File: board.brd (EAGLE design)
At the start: 69.8 x 50.8 mm, 85 parts, among them J1 AVR_SPI_PRG_6NS, U1 VS1063DS, U2 USD-SOCKETNEW, U3 MAX1555, U4 TPS2112A, U6 74HC595, U7 3.3V, U8 1.8V, Y1 12.288MHz, Y2 8MHz

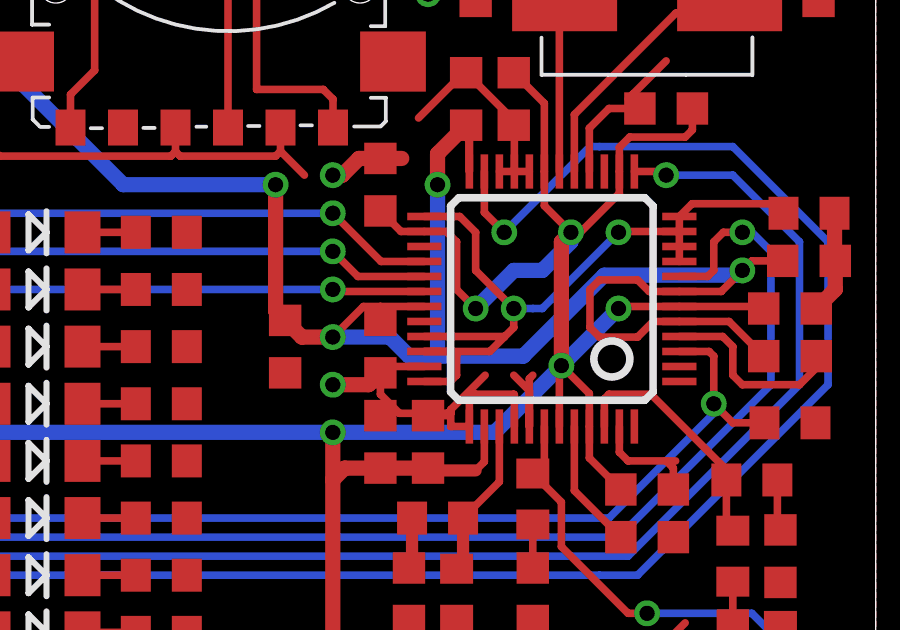
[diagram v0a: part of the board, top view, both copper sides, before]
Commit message: Connected XTest on vs1063 to VDD
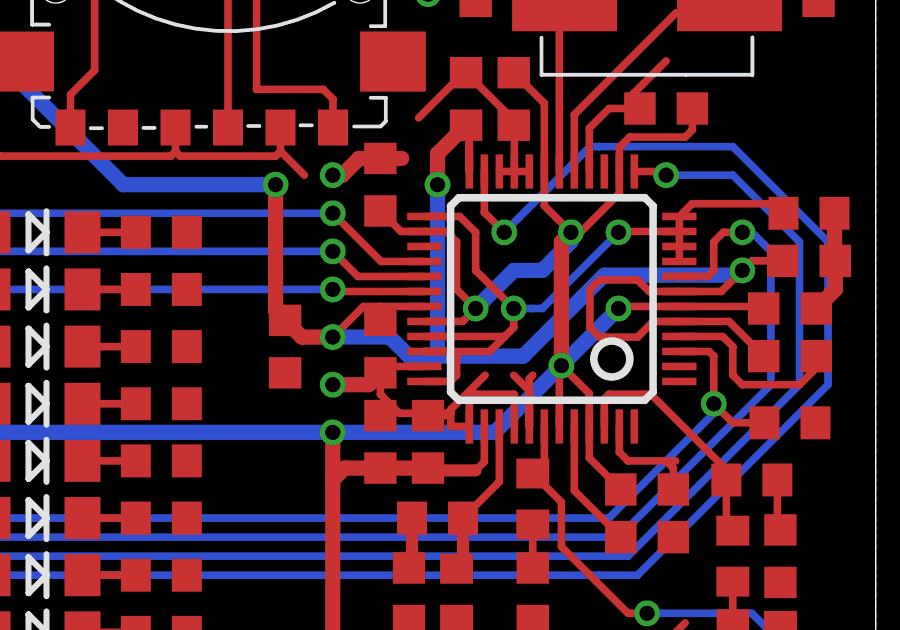
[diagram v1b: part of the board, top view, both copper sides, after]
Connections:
- removed net MP3_XTEST: U1.32
- net VDD: now also U1.32
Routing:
- net VDD: track 199.8 -> 201.7 mm
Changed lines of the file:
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@@
 <wire x1="30.695" y1="23.1775" x2="30.7975" y2="23.1775" width="0.254" layer="1"/>
 <wire x1="30.7975" y1="23.1775" x2="30.7975" y2="24.525" width="0.254" layer="1"/>
+<contactref element="U1" pad="32"/>
+<wire x1="54.805" y1="28.46" x2="56.0825" y2="28.46" width="0.254" layer="1"/>
+<wire x1="56.0825" y1="28.46" x2="56.515" y2="28.8925" width="0.254" layer="1"/>
 </signal>
 <signal name="GPIO">
@@
 <wire x1="28.995" y1="23.05" x2="28.995" y2="23.1775" width="0.254" layer="1"/>
 </signal>
-<signal name="MP3_XTEST">
-<contactref element="U1" pad="32"/>
-</signal>
 </signals>

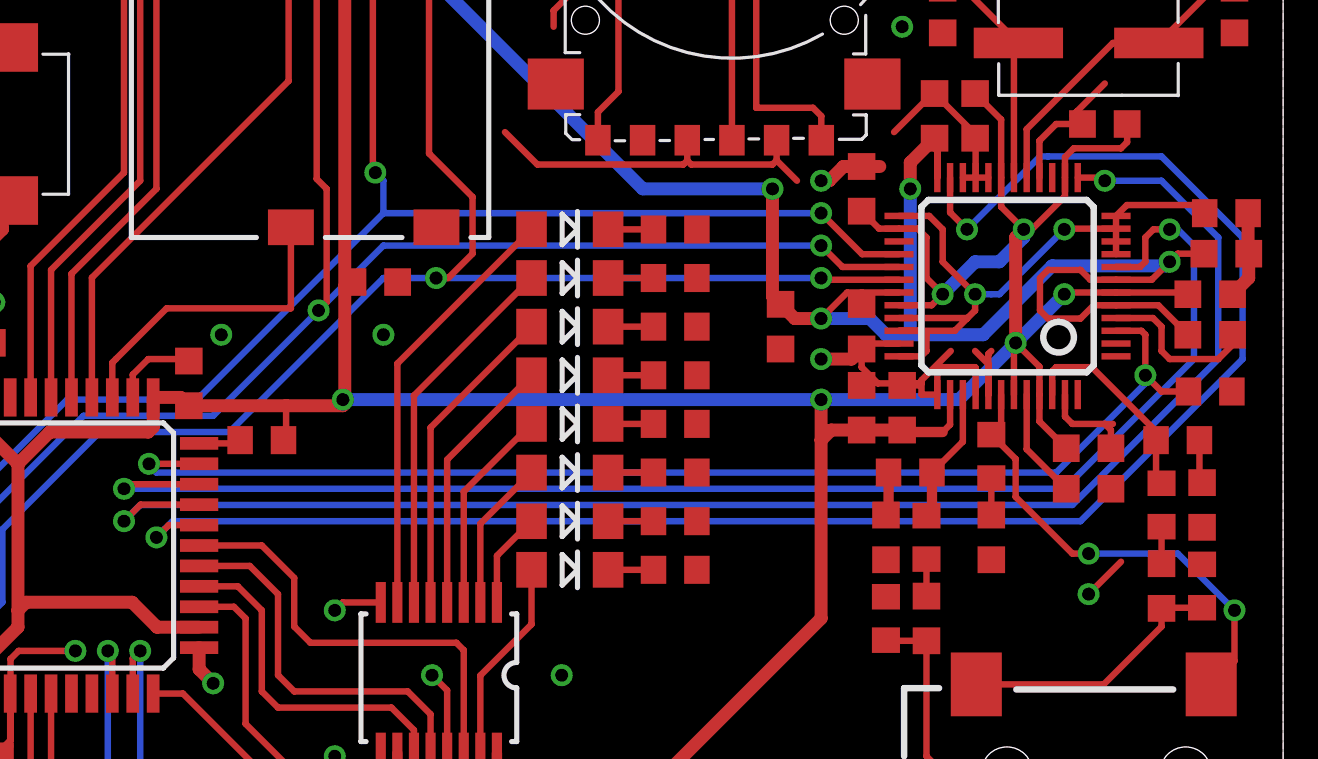
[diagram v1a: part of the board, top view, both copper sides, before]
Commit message: Added pull-ups to mp3 cs lines
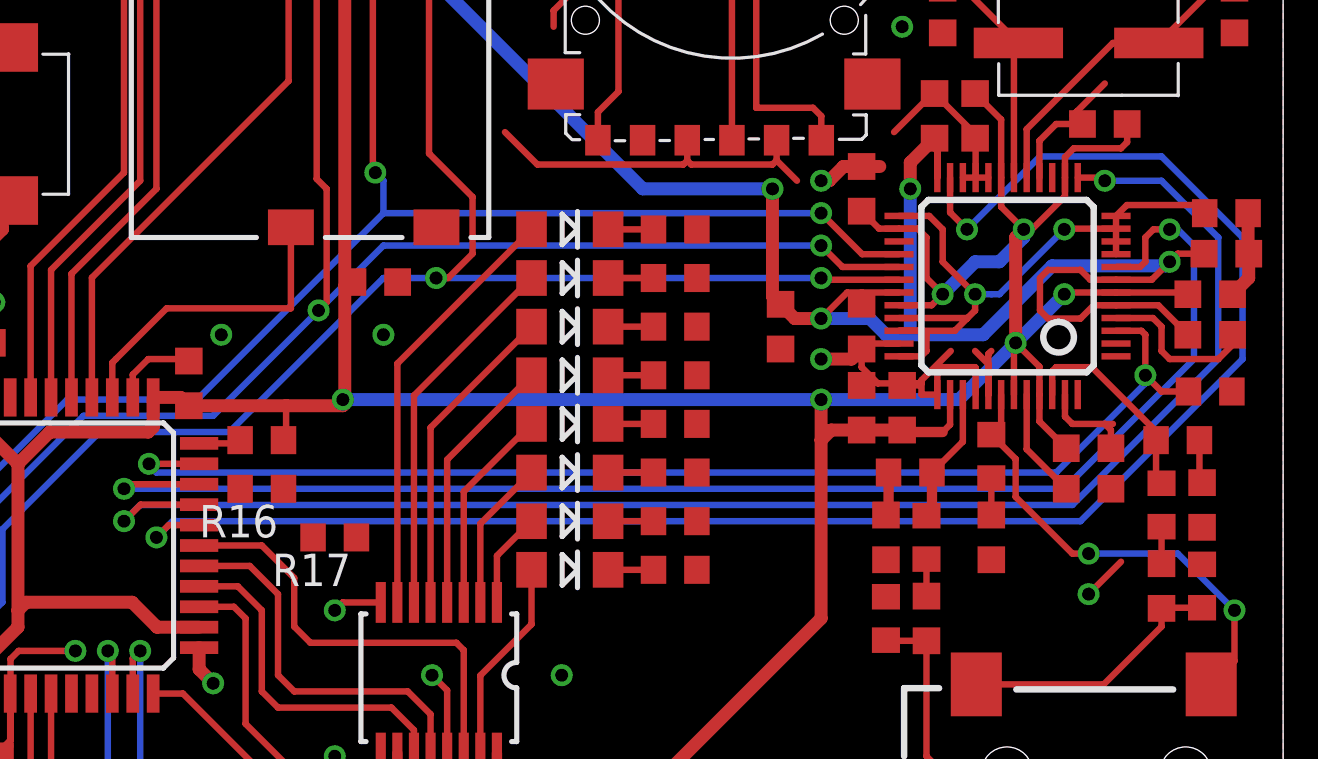
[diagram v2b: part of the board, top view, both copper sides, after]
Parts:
- added R16, R17: 10k, rcl:R0603W
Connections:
- net MP3_XCS: now also R16.1
- net MP3_XDCS: now also R17.1
- net VDD: now also R16.2, R17.2
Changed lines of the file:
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@@
 <element name="R14" library="rcl" package="R0603" value="10k" x="29.845" y="23.1775" smashed="yes" rot="R180"/>
 <element name="C33" library="rcl" package="C0603K" value="1u" x="50.165" y="27.6225" smashed="yes" rot="R270"/>
+<element name="R16" library="rcl" package="R0603W" value="10k" x="29.845" y="21.2725" rot="R180"/>
+<element name="R17" library="rcl" package="R0603W" value="10k" x="32.7025" y="19.3675" rot="R180"/>
 </elements>
 <signals>
@@
 <wire x1="54.805" y1="28.46" x2="56.0825" y2="28.46" width="0.254" layer="1"/>
 <wire x1="56.0825" y1="28.46" x2="56.515" y2="28.8925" width="0.254" layer="1"/>
+<contactref element="R17" pad="2"/>
+<contactref element="R16" pad="2"/>
+<wire x1="28.995" y1="21.2725" x2="31.8525" y2="19.3675" width="0" layer="19" extent="1-1"/>
+<wire x1="30.695" y1="23.1775" x2="28.995" y2="21.2725" width="0" layer="19" extent="1-1"/>
 </signal>
 <signal name="GPIO">
@@
 <wire x1="56.805" y1="32.095" x2="57.4675" y2="31.4325" width="0.254" layer="1"/>
 <via x="57.4675" y="31.4325" extent="1-16" drill="0.508"/>
-<wire x1="60.6425" y1="34.29" x2="65.0875" y2="34.29" width="0.254" layer="16"/>
+<wire x1="60.325" y1="34.29" x2="65.0875" y2="34.29" width="0.254" layer="16"/>
 <wire x1="65.0875" y1="34.29" x2="68.2625" y2="31.115" width="0.254" layer="16"/>
 <wire x1="68.2625" y1="31.115" x2="68.2625" y2="26.3525" width="0.254" layer="16"/>
@@
 <wire x1="26.2" y1="19.85" x2="25.7175" y2="19.3675" width="0.254" layer="1"/>
 <via x="25.7175" y="19.3675" extent="1-16" drill="0.508"/>
-<wire x1="25.7175" y1="19.3675" x2="26.035" y2="19.685" width="0.254" layer="16"/>
-<wire x1="26.035" y1="19.685" x2="26.3525" y2="20.0025" width="0.254" layer="16"/>
-<wire x1="26.3525" y1="20.0025" x2="60.6425" y2="20.0025" width="0.254" layer="16"/>
-<wire x1="60.6425" y1="20.0025" x2="61.9125" y2="20.0025" width="0.254" layer="16"/>
+<wire x1="25.7175" y1="19.3675" x2="26.3525" y2="20.0025" width="0.254" layer="16"/>
+<wire x1="26.3525" y1="20.0025" x2="61.9125" y2="20.0025" width="0.254" layer="16"/>
 <wire x1="61.9125" y1="20.0025" x2="68.2625" y2="26.3525" width="0.254" layer="16"/>
-<wire x1="60.6425" y1="34.29" x2="60.325" y2="34.29" width="0.254" layer="16"/>
 <wire x1="60.325" y1="34.29" x2="57.4675" y2="31.4325" width="0.254" layer="16"/>
+<contactref element="R16" pad="1"/>
+<wire x1="27.39" y1="19.85" x2="30.695" y2="21.2725" width="0" layer="19" extent="1-1"/>
 </signal>
 <signal name="MP3_XDCS">
@@
 <wire x1="27.39" y1="20.65" x2="25.095" y2="20.65" width="0.254" layer="1"/>
 <wire x1="25.095" y1="20.65" x2="24.4475" y2="20.0025" width="0.254" layer="1"/>
+<contactref element="R17" pad="1"/>
+<wire x1="27.39" y1="20.65" x2="33.5525" y2="19.3675" width="0" layer="19" extent="1-1"/>
 </signal>
 <signal name="MP3_DREQ">

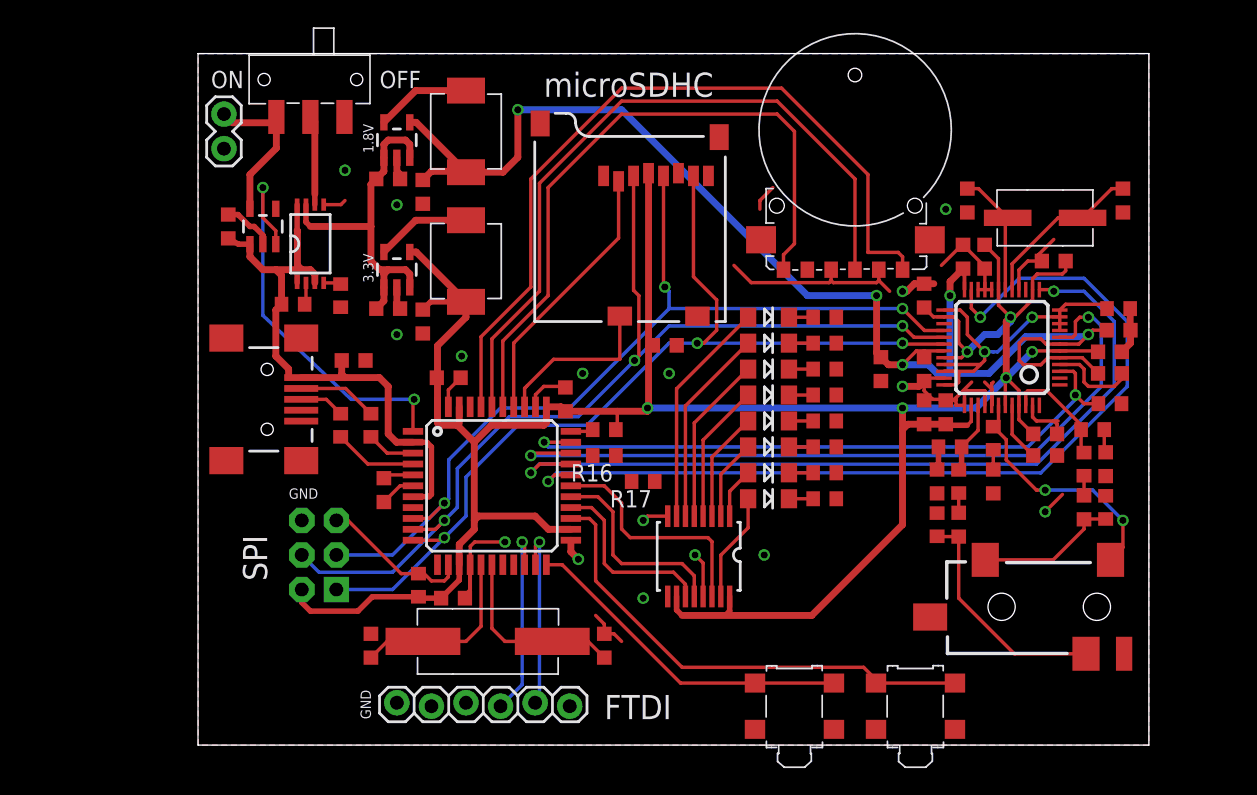
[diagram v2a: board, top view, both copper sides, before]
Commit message: Beginning to switch to atmega32u2
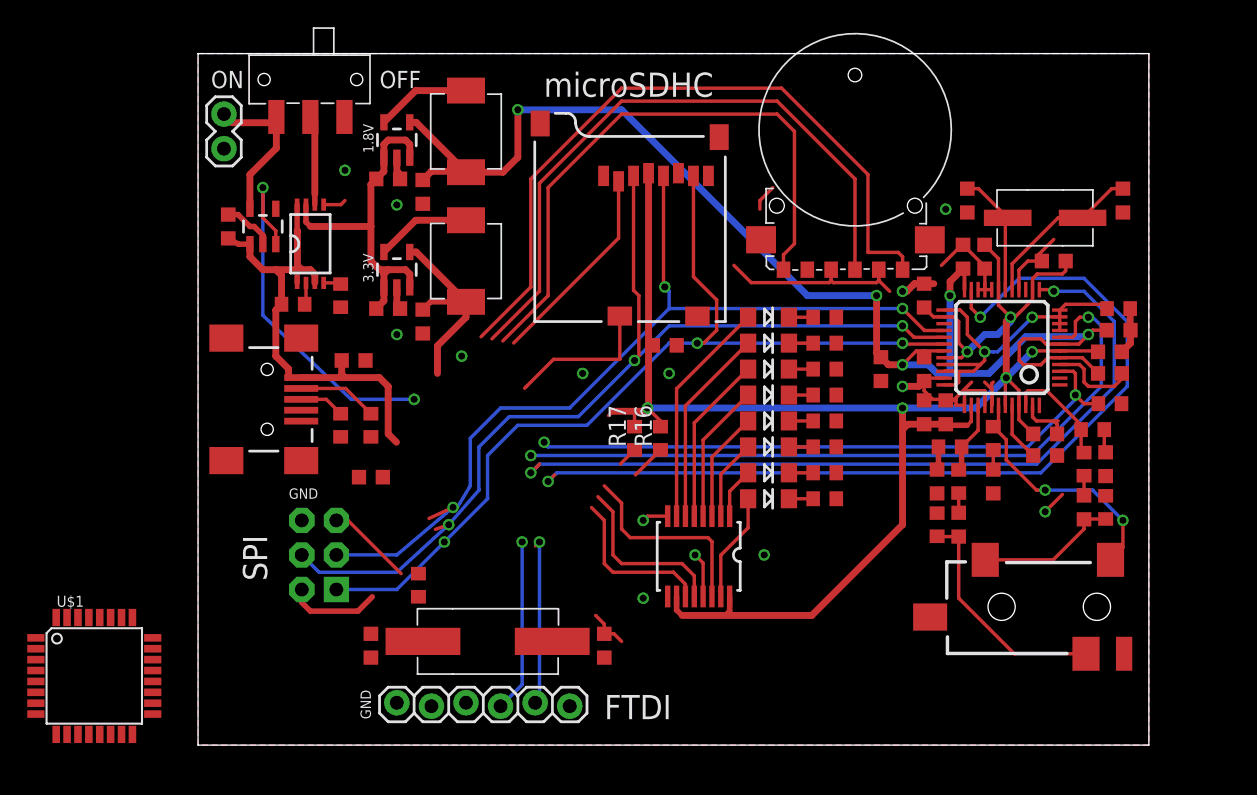
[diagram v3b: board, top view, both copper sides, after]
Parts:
- removed C23, C24, C32: 0.1u, rcl:C0603K
- removed R14: 10k, rcl:R0603
- removed S2, S3: EVQ-PSC, mkmp3:EVQ-PSQ
- removed U$2: ATMEGA32U4TQFP, SparkFun-DigitalIC:SPARKFUN-DIGITALIC_TQFP44
- added U$1: ATMEGA32U2, CEDT:TQFP32-08
- moved R16 4.32 mm to (34.0, 22.5), turned to 90 degrees
- moved R17 3.24 mm to (32.1, 22.5), turned to 90 degrees
- moved C17 1.35 mm to (12.7, 19.7), turned to 0 degrees
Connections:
- removed net N$15: JP2.3, U$2.20
- removed net N$16: JP2.2, U$2.21
- removed net N$38: R14.2, U$2.33
- removed net N$9: C17.1, U$2.6
- removed net SWITCH1: S2.A, S2.A', U$2.22
- removed net SWITCH2: S3.A, S3.A', U$2.25
- new net SERIAL_RX: JP2.3, U$1.8
- new net SERIAL_TX: JP2.2, U$1.9
- net CHG_B: no longer U$2.1
- net DS: no longer U$2.28
- net ENCODER_A: no longer U$2.38
- net ENCODER_B: no longer U$2.40
- net ENCODER_S: no longer U$2.39
- net GND: now also U$1.28, U$1.3; no longer C23.2, C24.2, C32.2, S2.B, S2.B', S3.B, S3.B', U$2.15, U$2.23, U$2.35, U$2.43, U$2.5
- net MISO: now also U$1.17; no longer U$2.11
- net MOSI: now also U$1.16; no longer U$2.10
- net MP3_DREQ: no longer U$2.31
- net MP3_XCS: no longer U$2.29
- net MP3_XDCS: no longer U$2.30
- net MP3_XRESET: no longer U$2.32
- net N$14: now also U$1.2, Y2.P$1; no longer U$2.16, Y2.P$2
- net N$2: now also U$1.1, Y2.P$2; no longer U$2.17, Y2.P$1
- net RESET: now also R11.1, U$1.24; no longer R11.2, U$2.13
- net SCK: now also U$1.15; no longer U$2.9
- net SD_CD: no longer U$2.36
- net SD_CS: now also U$1.14; no longer U$2.37
- net SHCP: no longer U$2.26
- net STCP: no longer U$2.27
- net USB_D+: no longer U$2.4
- net USB_D-: no longer U$2.3
- net VBUS: now also U$1.31; no longer U$2.2, U$2.7
- net VDD: now also C17.1, R11.2, U$1.27, U$1.32, U$1.4; no longer C23.1, C24.1, C32.1, R11.1, R14.1, U$2.14, U$2.24, U$2.34, U$2.42, U$2.44
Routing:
- net VDD: track 201.7 -> 157.8 mm
- net SWITCH2: track 35.8 -> 0.00 mm
- net SWITCH1: track 24.7 -> 0.00 mm
- net GND: track 102.9 -> 83.9 mm, vias 16 -> 14
- net N$15: track 14.5 -> 0.00 mm, vias 1 -> 0
- net N$2: track 13.8 -> 0.00 mm
- net N$16: track 13.7 -> 0.00 mm, vias 1 -> 0
- net N$14: track 13.6 -> 0.00 mm
- net SERIAL_RX: track 0.00 -> 13.0 mm, vias 0 -> 1
- net SERIAL_TX: track 0.00 -> 12.4 mm, vias 0 -> 1
- net VBUS: track 44.0 -> 36.4 mm
- net USB_D+: track 6.14 -> 0.00 mm
- net ENCODER_B: track 57.8 -> 52.6 mm
- net ENCODER_S: track 52.6 -> 47.6 mm
- net ENCODER_A: track 48.8 -> 44.0 mm
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
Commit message: Switched to smaller uC and VS1003 chip
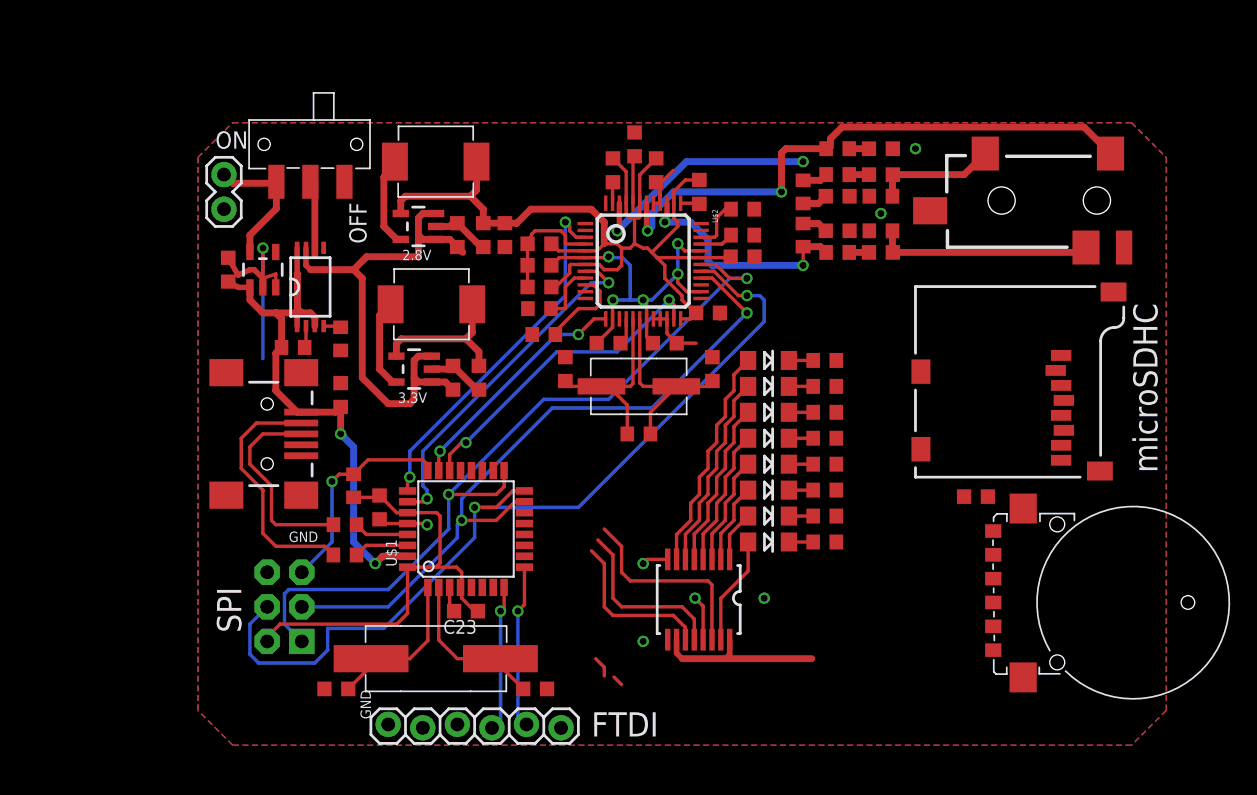
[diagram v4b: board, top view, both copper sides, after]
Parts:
- removed C31: 10u, rcl:C0603K
- removed U1: VS1063DS, mkmp3:LQFP-48
- added C23: 0.1u, rcl:C0603K
- added R14: 100k, rcl:R0603W
- added U$2: VS1003, mkmp3:LQFP-48
- R1: value 100k -> 1M
- R15: value 10k -> 100k; device rcl:R0603W -> rcl:R0603
- R16, R17: value 10k -> 100k
- U8: value 1.8V -> 2.8V
- moved C9 43.0 mm to (25.1, 36.8), turned to 180 degrees
- moved C6 42.2 mm to (25.1, 33.7), turned to 180 degrees
- moved C4 39.2 mm to (25.1, 35.2), turned to 180 degrees
- moved C1 37.8 mm to (32.1, 44.1), turned to 90 degrees
- moved R1 36.4 mm to (32.4, 22.9), turned to 0 degrees
- moved C20 32.6 mm to (37.8, 27.6), turned to 90 degrees
- moved Y1 32.3 mm to (32.4, 26.4)
- moved C19 32.0 mm to (27.0, 27.6), turned to 90 degrees
- moved R15 30.5 mm to (40.0, 39.4)
- moved U5 29.8 mm to (69.5, 40.0)
- moved U$1 29.4 mm to (19.7, 15.9), turned to 90 degrees
- moved C33 29.3 mm to (22.5, 37.5)
- moved C2 29.2 mm to (34.3, 29.5), turned to 0 degrees
- moved C16 28.6 mm to (50.2, 41.9), turned to 0 degrees
- moved C8 28.3 mm to (40.0, 35.9)
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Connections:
- removed net GPIO: R1.2, U1.10, U1.11, U1.12, U1.25, U1.33, U1.34, U1.36, U1.9
- new net GPIO0: R14.2, U$2.33
- new net GPIO1: R15.2, U$2.34
- new net GPIO2: R16.2, U$2.9
- new net GPIO3: R17.2, U$2.10
- net CVDD: now also C5.1, C6.1, C7.1, U$2.24, U$2.31, U$2.38, U$2.43, U$2.45, U$2.5, U$2.7; no longer U1.24, U1.31, U1.5, U1.7
- net GBUF: now also U$2.42; no longer U1.42
- net GND: now also C23.2, R14.1, R16.1, R17.1, U$2.16, U$2.20, U$2.21, U$2.22, U$2.37, U$2.4, U$2.40, U$2.41, U$2.47; no longer C31.2, R1.1, U1.16, U1.20, U1.21, U1.22, U1.35, U1.37, U1.4, U1.40, U1.41, U1.47
- net LEFT: now also U$2.46; no longer U1.46
- net MISO: now also U$2.30; no longer U1.30
- net MOSI: now also U$2.29; no longer U1.29
- net MP3_DREQ: now also U$1.26, U$2.8; no longer U1.8
- net MP3_XCS: now also U$1.22, U$2.23; no longer R16.1, U1.23
- net MP3_XDCS: now also U$1.23, U$2.13; no longer R17.1, U1.13
- net MP3_XRESET: now also U$1.25, U$2.3; no longer R15.2, U1.3
- net N$7: now also R1.2, U$2.18; no longer U1.17
- net N$8: now also R1.1, U$2.17; no longer U1.18
- net RCAP: now also U$2.44; no longer U1.44
- net RIGHT: now also U$2.39; no longer U1.39
- net SCK: now also U$2.28; no longer U1.28
- net USB_D+: now also U$1.29
- net USB_D-: now also U$1.30
- net VDD: now also C23.1, U$2.14, U$2.19, U$2.26, U$2.32, U$2.6; no longer C31.1, C5.1, C6.1, C7.1, R16.2, R17.2, U1.14, U1.19, U1.26, U1.32, U1.38, U1.43, U1.45, U1.6
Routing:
- net VDD: track 157.8 -> 88.9 mm, vias 6 -> 5
- net ENCODER_B: track 52.6 -> 0.00 mm
- net ENCODER_S: track 47.6 -> 0.00 mm
- net MP3_XCS: track 69.1 -> 23.5 mm
- net ENCODER_A: track 44.0 -> 0.00 mm
- net MP3_XDCS: track 59.1 -> 17.7 mm
- net GND: track 83.9 -> 51.8 mm, vias 14 -> 7
- net CVDD: track 101.4 -> 71.1 mm, vias 5 -> 0
- net MP3_DREQ: track 53.2 -> 26.0 mm
- net GPIO: track 26.4 -> 0.00 mm, vias 2 -> 0
- net GBUF: track 18.5 -> 42.6 mm
- net MP3_XRESET: track 45.7 -> 26.7 mm
- net CHG_B: track 27.6 -> 12.3 mm, vias 2 -> 1
- net SD_CS: track 15.1 -> 0.00 mm
- net SCK: track 66.8 -> 52.7 mm, vias 3 -> 2
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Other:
- board outline removed
